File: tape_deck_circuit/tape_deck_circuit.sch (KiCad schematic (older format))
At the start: 5 parts

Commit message: Continue sketching out
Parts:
- added C? (x3): 0.1uF, symbol Device:C_Small
- added D?: 1N914, symbol Device:D_Small
- added J?: DIN-5_180degree, symbol Connector:DIN-5_180degree
- added J?: MIDI IN, symbol Connector_Generic:Conn_01x04
- added R?: 220, symbol Device:R
- added U?: MCP41HVx1, symbol midi_tape_deck:MCP41HVx1
- added U?: 6N138, symbol Isolator:6N138
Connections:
- net +15V: now also U?.14 (V+)
- net +5V: now also A?.27 (+5V), C?.2, U?.1 (VL), U?.8 (VCC)
- net GND: now also A?.29 (GND), A?.4 (GND), C?.1, C?.1, C?.1, U?.10 (V-), U?.3 (~CS), U?.5 (GND), U?.7 (~SHDN), U?.8 (DGND), U?.9 (NC)
- net MIDI_OUT: now reaches A?.1 (D1/TX)
- net ~LATCH: now reaches A?.12 (D9)
- net ~LATCH: now also U?.6 (~WLAT)
- net MOSI: now reaches A?.14 (D11)
- net MOSI: now also U?.4 (SDI)
- net MISO: now reaches A?.15 (D12)
- net MISO: now also U?.5 (SDO)
- net SCK: now reaches A?.16 (D13)
- net SCK: now also U?.2 (SCK)
- net MIDI_IN: now reaches A?.2 (D0/RX)
- net MIDI_IN: now also U?.6 (VO2)
- net INT0: now reaches A?.5 (D2)
- net INT1: now reaches A?.6 (D3)
- new net: D?.1 (K), R?.1, U?.2 (C1)
- new net PIN2: C?.2, J?.3 (Pin_3)
- new net PIN4: J?.1 (Pin_1), R?.2
- new net PIN5: D?.2 (A), J?.2 (Pin_2), U?.3 (C2)
- new net SHELL: C?.2, J?.4 (Pin_4)
- no-connect marks 0 -> 11
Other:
- moved on the sheet: A?, J?, RV1, RV2

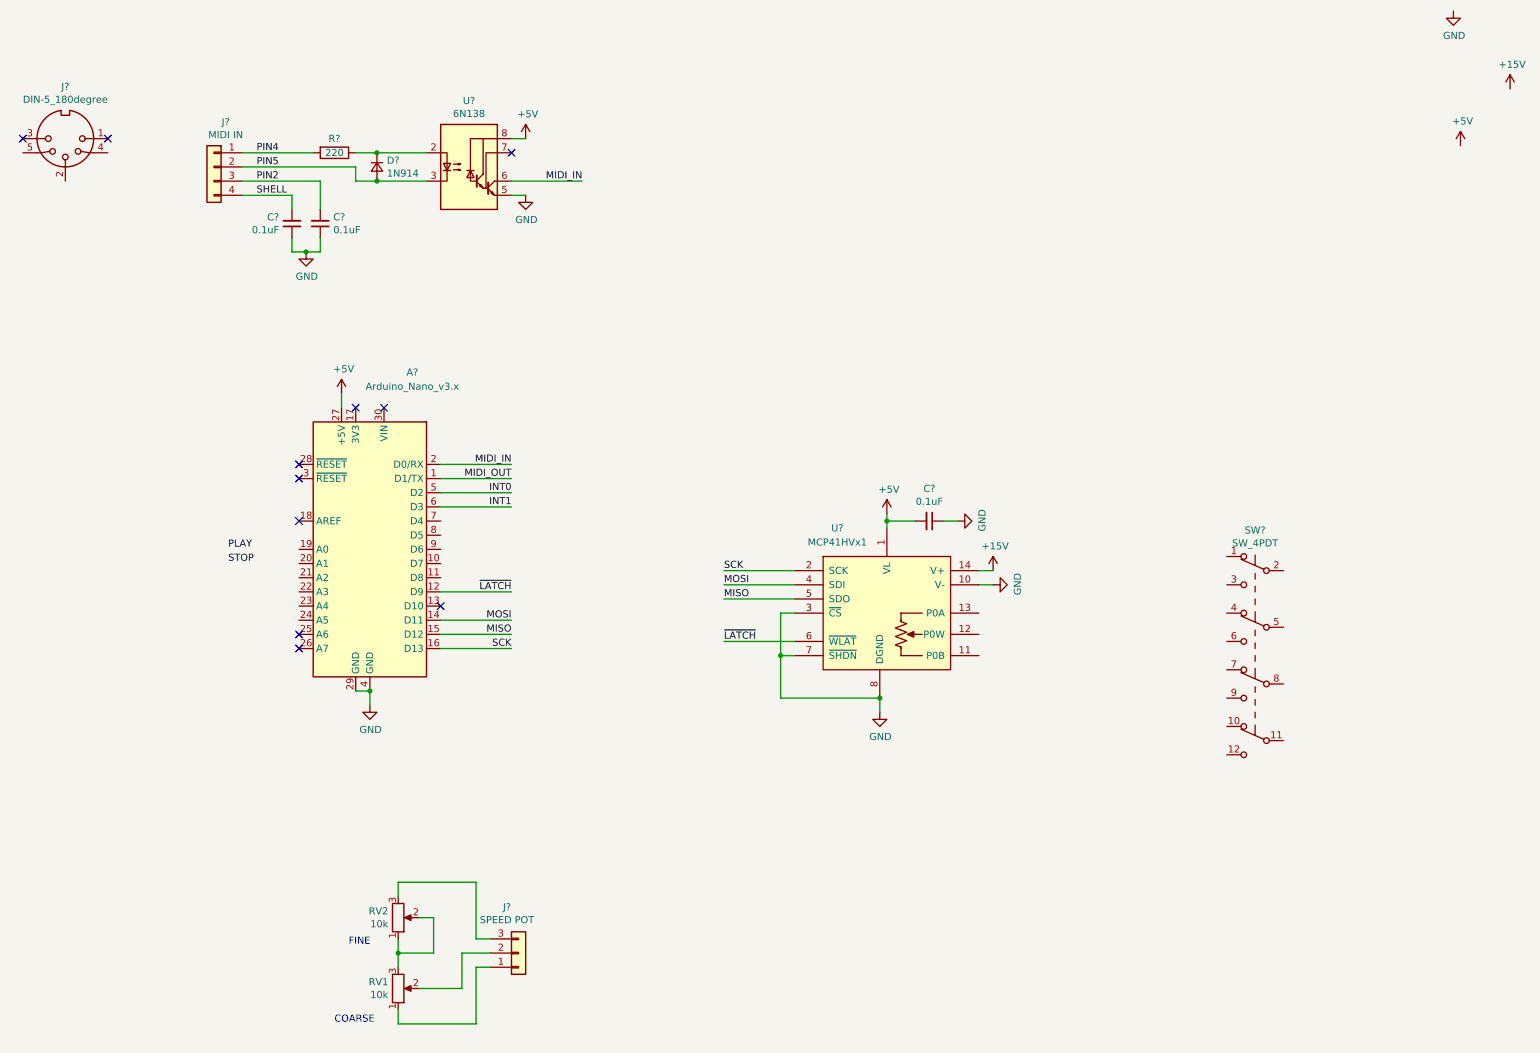
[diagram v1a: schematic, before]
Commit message: Complete basic schematic
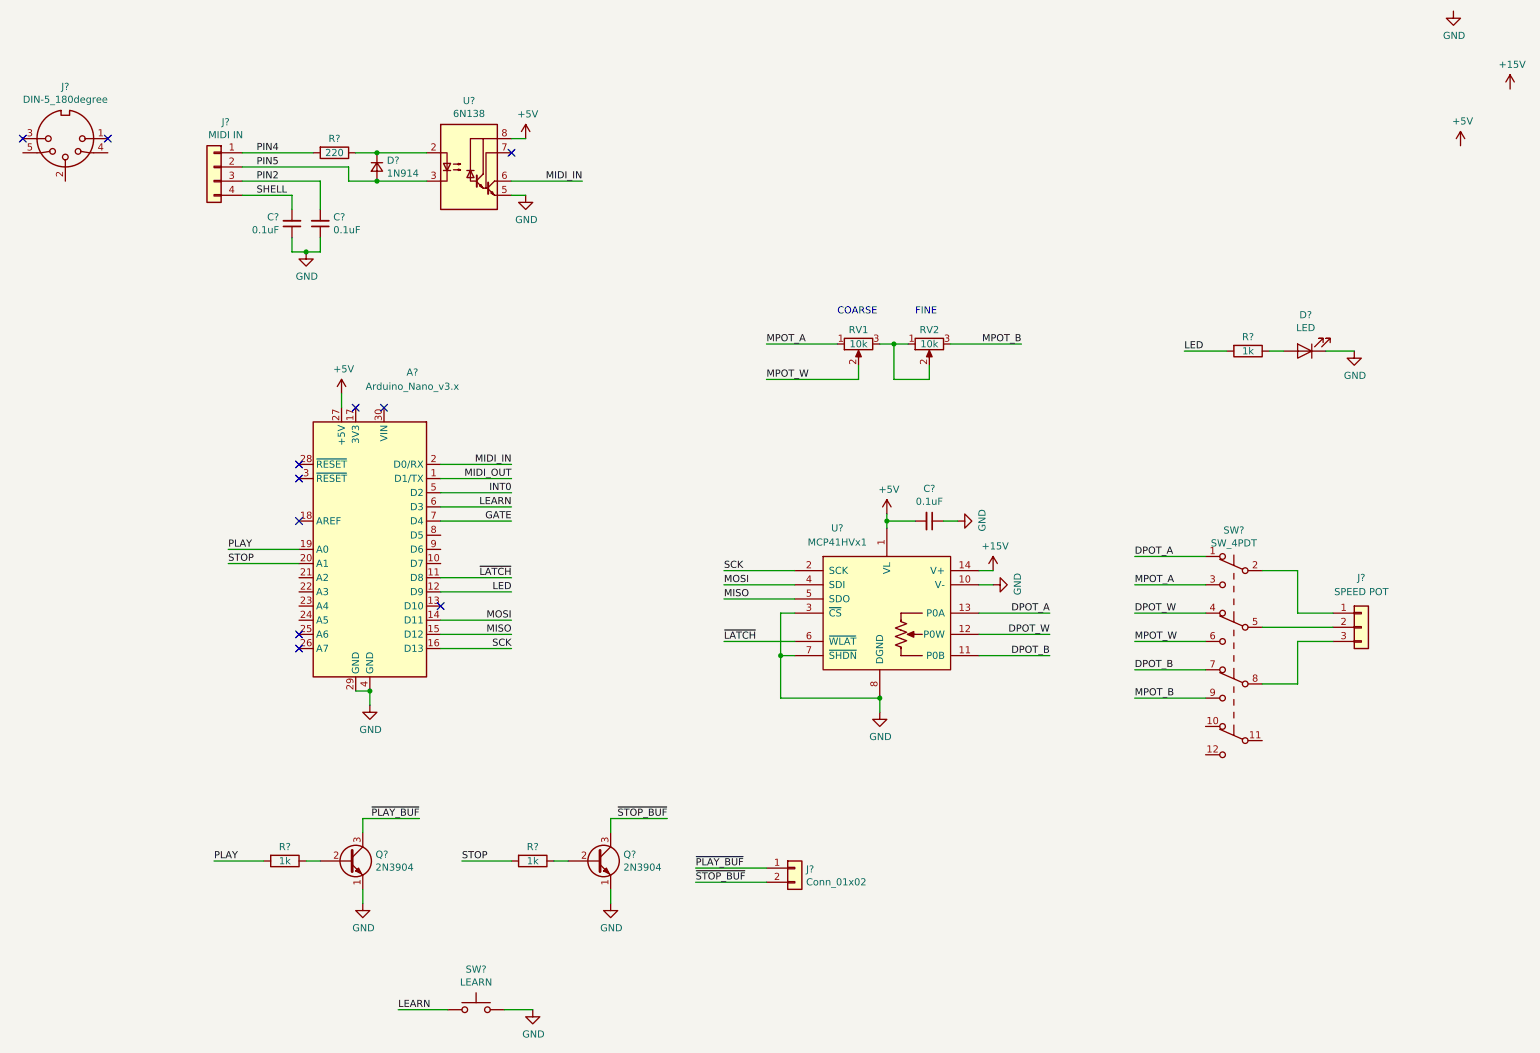
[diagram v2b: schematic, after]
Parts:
- added D?: LED, symbol Device:LED
- added J?: Conn_01x02, symbol Connector_Generic:Conn_01x02
- added Q? (x2): 2N3904, symbol Device:Q_NPN_EBC
- added R? (x3): 1k, symbol Device:R
- added SW?: LEARN, symbol Switch:SW_Push
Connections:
- net GND: now also D?.1 (K), Q?.1 (E), Q?.1 (E), SW?.2
- net PLAY: now also A?.19 (A0), R?.2
- net STOP: now also A?.20 (A1), R?.2
- net ~LATCH: now also A?.11 (D8); no longer A?.12 (D9)
- net GATE: now reaches A?.7 (D4)
- net at J?.1 (Pin_1): now also SW?.2 (B); no longer RV1.1
- net at J?.2 (Pin_2): now also SW?.5 (B); no longer RV1.2
- net at J?.3 (Pin_3): now also SW?.8 (B); no longer RV2.3
- net DPOT_A: now reaches SW?.1 (A)
- net DPOT_A: now also U?.13 (P0A)
- net MPOT_A: now reaches SW?.3 (C)
- net MPOT_A: now also RV1.1
- net DPOT_W: now reaches SW?.4 (A)
- net DPOT_W: now also U?.12 (P0W)
- net MPOT_W: now reaches SW?.6 (C)
- net MPOT_W: now also RV1.2
- net DPOT_B: now reaches SW?.7 (A)
- net DPOT_B: now also U?.11 (P0B)
- net MPOT_B: now reaches SW?.9 (C)
- net MPOT_B: now also RV2.3
- net INT1 renamed LEARN
- net LEARN: now also SW?.1
- new net: D?.2 (A), R?.1
- new net: Q?.2 (B), R?.1 (x2)
- new net LED: A?.12 (D9), R?.2
- new net ~PLAY_BUF: J?.1 (Pin_1), Q?.3 (C)
- new net ~STOP_BUF: J?.2 (Pin_2), Q?.3 (C)
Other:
- moved on the sheet: J?, RV1, RV2, SW?

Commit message: Fix SHDN signal on digipot
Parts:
- A?: symbol MCU_Module:Arduino_Nano_v3.x -> tape_deck_circuit-rescue:Arduino_Nano_v3.x-MCU_Module
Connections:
- net +5V: now also U?.7 (~SHDN)
- net GND: now also U?.6 (~WLAT); no longer U?.7 (~SHDN)
- net ~LATCH: no longer U?.6 (~WLAT)
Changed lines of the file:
@@
 EESchema Schematic File Version 4
+LIBS:tape_deck_circuit-cache
 EELAYER 30 0
 EELAYER END
@@
 $EndDescr
 $Comp
-L MCU_Module:Arduino_Nano_v3.x A?
+L tape_deck_circuit-rescue:Arduino_Nano_v3.x-MCU_Module A?
 U 1 1 6105AC23
 P 2200 3950
@@
 $EndComp
 Wire Wire Line
-	5200 4700 5100 4700
-Wire Wire Line
-	5100 4700 5100 5000
-Wire Wire Line
 	5100 5000 5800 5000
 Wire Wire Line
@@
 	5200 4400 5100 4400
 Wire Wire Line
-	5100 4400 5100 4700
-Connection ~ 5100 4700
+	5100 4400 5100 4600
 $Comp
 L power:+15V #PWR?
@@
 Wire Wire Line
 	2700 4150 3200 4150
-Text Label 4700 4600 0    50   ~ 0
-~LATCH
-Wire Wire Line
-	4700 4600 5200 4600
 Text Label 1200 3950 0    50   ~ 0
 PLAY
@@
 Wire Wire Line
 	2700 3750 3200 3750
+Wire Wire Line
+	5200 4600 5100 4600
+Connection ~ 5100 4600
+Wire Wire Line
+	5100 4600 5100 5000
+$Comp
+L power:+5V #PWR?
+U 1 1 610A8E36
+P 4900 4700
+F 0 "#PWR?" H 4900 4550 50  0001 C CNN
+F 1 "+5V" H 4915 4873 50  0000 C CNN
+F 2 "" H 4900 4700 50  0001 C CNN
+F 3 "" H 4900 4700 50  0001 C CNN
+	1    4900 4700
+	1    0    0    -1
+$EndComp
+Wire Wire Line
+	4900 4700 5200 4700
 $EndSCHEMATC
